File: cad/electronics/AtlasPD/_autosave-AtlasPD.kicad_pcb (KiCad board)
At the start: 2 copper layers, 37.4 x 20 mm, 41 parts, among them J1 Conn_01x02_Male, J2 Conn_01x02_Male, J2 USB_C_Receptacle_USB2.0, SW1 SW_MEC_5E, U1 LM2678T-ADJ_NOPB, U2 ATmega328P-AU, U4 CP2104, U5 AMS1117-3.3, Y1 CSTNE16M0V53-R0

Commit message: More Electronics design work
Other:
- copper layers 2 -> 4
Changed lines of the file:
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@@
   (layers
     (0 F.Cu signal)
+    (1 In1.Cu signal)
+    (2 In2.Cu signal)
     (31 B.Cu signal)
     (32 B.Adhes user)
@@
     (46 B.CrtYd user)
     (47 F.CrtYd user)
-    (48 B.Fab user hide)
-    (49 F.Fab user hide)
+    (48 B.Fab user)
+    (49 F.Fab user)
   )
   (setup

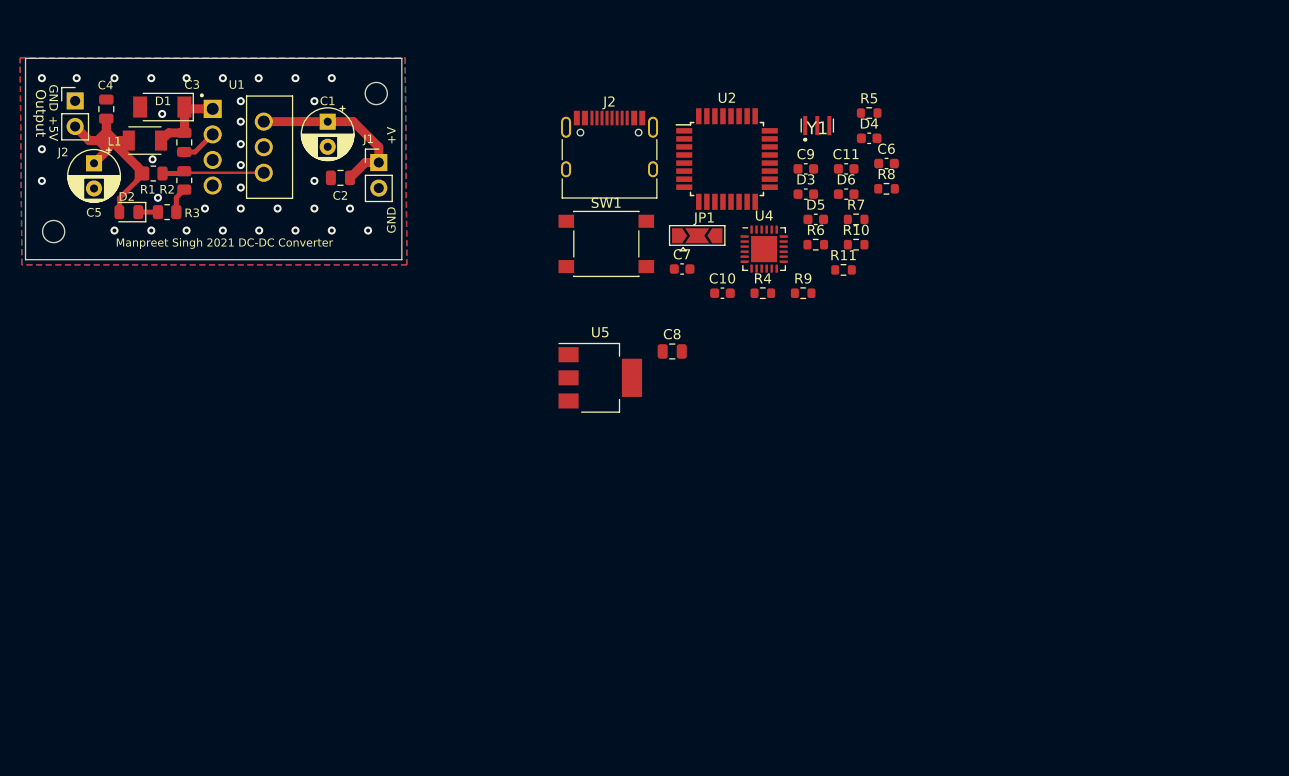
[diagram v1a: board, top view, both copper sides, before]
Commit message: Started layout
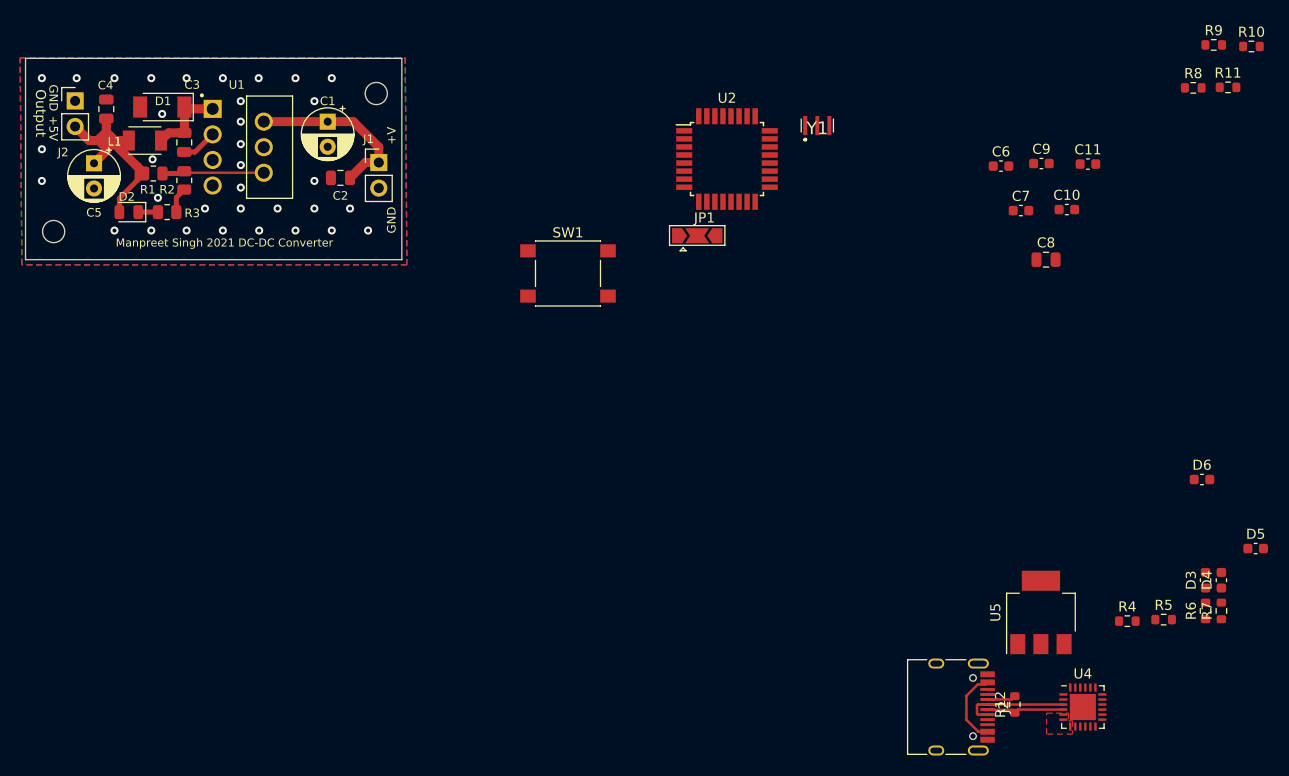
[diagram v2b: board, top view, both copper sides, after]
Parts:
- added R12: 0, Resistor_SMD:R_0603_1608Metric, F.Cu at (120.3, 81.3)
- SW1: value SW_MEC_5E -> SW_SPST
- moved J2 64.0 mm to (113.6, 81.5), turned to 270 degrees
- moved R5 58.2 mm to (135.1, 72.8)
- moved D4 56.2 mm to (140.9, 68.9), turned to 90 degrees
- moved U4 55.4 mm to (127.1, 81.5)
- moved D3 55.2 mm to (139.3, 68.9), turned to 90 degrees
- moved D5 54.6 mm to (144.3, 65.8)
- moved R7 53.2 mm to (140.9, 72.0), turned to 90 degrees
- moved R6 53.1 mm to (139.3, 72.0), turned to 90 degrees
- moved U5 49.6 mm to (122.9, 72.1), turned to 90 degrees
- moved R4 48.7 mm to (131.5, 73.0)
- moved R9 47.7 mm to (140.1, 15.7)
- moved D6 45.3 mm to (138.9, 58.9)
- moved R10 43.9 mm to (143.9, 15.9)
- moved R11 42.3 mm to (141.5, 20.0)
- moved C8 38.2 mm to (123.4, 37.1)
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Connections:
- J2 pad B7: /Sheet60A2E58A/USB_DN -> Net-(J2-PadB7)
- SW1 pad 2: Net-(C11-Pad2) -> GND
- U4 pad 20: /Sheet60A2E58A/IO1 -> /Sheet60A2E58A/RXD
- Y1 pad 1: Net-(Y1-Pad1) -> Net-(U2-Pad8)
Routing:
- net /Sheet60A2E58A/USB_DP: track 0.00 -> 10.9 mm
- net /Sheet60A2E58A/USB_DN: track 0.00 -> 7.80 mm
- net +5V: track 0.00 -> 7.62 mm
- net Net-(J2-PadB7): track 0.00 -> 2.85 mm
- added copper zone on F.Cu, net +3V3
